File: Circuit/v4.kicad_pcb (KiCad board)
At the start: 2 copper layers, 30 x 50 mm, 41 parts, among them J2 AVR-ISP-6, Q1 IRLML6244TRPBF, U1 HMHA2801AR2, U4 ATtiny841-SSU

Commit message: Version 4.2 complete
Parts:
- moved C2 2.76 mm to (126.7, 63.1)
- moved D1 2.76 mm to (126.7, 60.5)
- moved R5 0.89 mm to (117.2, 57.7)
- moved R16 0.80 mm to (114.1, 57.7)
- moved R19 0.60 mm to (105.8, 74.2)
- moved R6 0.60 mm to (109.6, 69.2)
- moved R7 0.60 mm to (109.6, 79.2)
- moved R8 0.60 mm to (105.1, 69.2)
- moved R9 0.60 mm to (105.1, 79.2)
- moved R10 0.60 mm to (105.1, 61.0)
- moved R12 0.60 mm to (109.6, 61.0)
- moved R11 0.60 mm to (105.1, 87.5)
- moved R13 0.60 mm to (109.6, 87.5)
- moved R20 0.60 mm to (109.4, 74.0)
- moved R17 0.41 mm to (106.9, 55.2)
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- renumbered U4 to ATTINY841
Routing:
- net Net-(Q1-Pad3): track 52.9 -> 39.3 mm, vias 3 -> 2
- net GND: track 56.1 -> 63.7 mm, vias 13 -> 19
- net Net-(ATTINY841-Pad3): track 32.7 -> 30.5 mm
- net DUMP_LOAD_ENABLE: track 16.3 -> 14.9 mm
- net Net-(ATTINY841-Pad2): track 25.2 -> 26.5 mm
- net Net-(ATTINY841-Pad7): track 58.1 -> 59.1 mm
- net 2_VOLT: track 67.3 -> 66.3 mm
- net TXD0: track 17.8 -> 18.5 mm
- net Net-(ATTINY841-Pad9): track 48.2 -> 47.6 mm
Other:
- board text added: "1 Jan 2020"
- board text added: "DIYBMS v4.2"
- board text added: "©2019/2020 Stuart Pittaway"
- board text removed: "20 Dec 2019"
- board text removed: "DIYBMS v4.1"
- board text removed: "©2019 Stuart Pittaway"

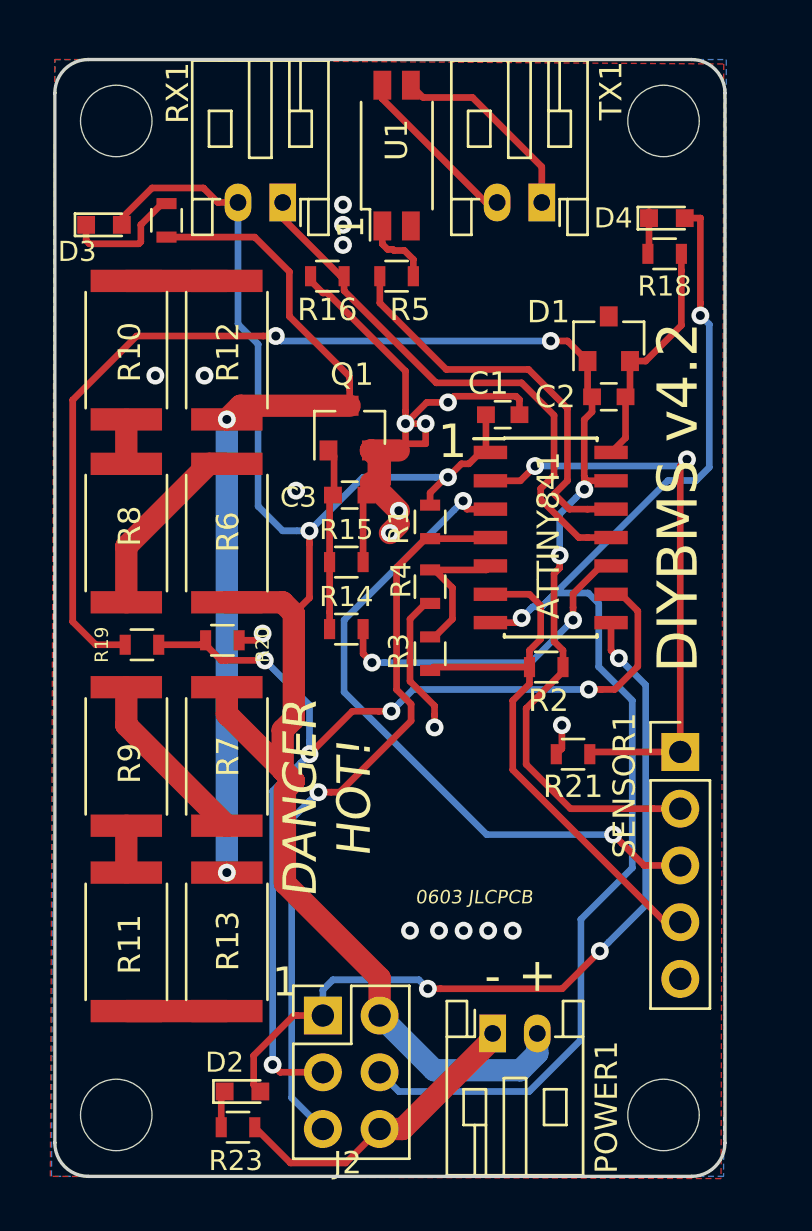
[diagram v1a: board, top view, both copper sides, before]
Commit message: Redesigned circuit using TCLT1003 optoisolator
For 30 boards
Charge Details
Engineering fee:$4.00
Board:$3.10
SMT Price:
Setup fee:$7.00
Stencil:$0.00
Panel:$0.00
Components:$37.27
Extended components fee:$15.00
Total Price:$66.37
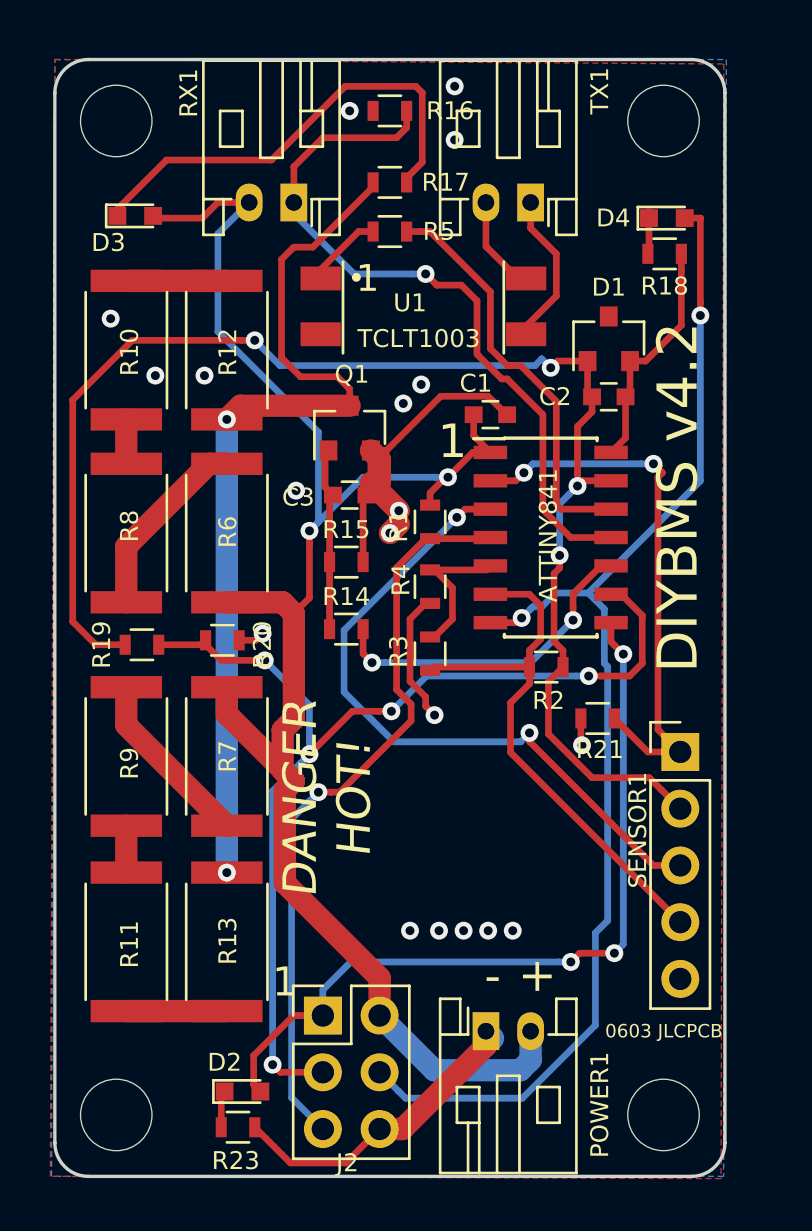
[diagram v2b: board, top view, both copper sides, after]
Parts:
- U1: value HMHA2801AR2 -> TCLT1003; footprint Housings_SSOP:SOP-4_4.4x2.8mm_Pitch1.27mm -> Circuit:SOP4-L-Pitch2.54
- moved R17 10.1 mm to (116.9, 53.5), turned to 0 degrees
- moved R16 7.91 mm to (116.9, 50.3)
- moved U1 6.94 mm to (118.6, 59.1), turned to 270 degrees
- moved R5 2.02 mm to (116.9, 55.7), turned to 0 degrees
- moved R21 1.94 mm to (126.2, 77.5)
- moved D3 1.46 mm to (105.5, 55.0)
- moved C1 0.55 mm to (121.4, 63.9)
- moved RX1 0.50 mm to (112.6, 54.4)
- moved TX1 0.50 mm to (123.2, 54.4)
- moved POWER1 0.32 mm to (121.2, 91.5)
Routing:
- net Net-(D3-Pad1): track 5.55 -> 20.6 mm
- net GND: track 63.7 -> 50.6 mm
- net RXD0: track 24.8 -> 32.7 mm, vias 0 -> 1
- net Net-(TX1-Pad2): track 7.67 -> 4.36 mm
- net Net-(ATTINY841-Pad7): track 59.1 -> 55.9 mm
- net Net-(TX1-Pad1): track 8.97 -> 6.94 mm
- net 2_VOLT: track 66.3 -> 64.5 mm
- net Net-(ATTINY841-Pad2): track 26.5 -> 24.7 mm
- net Net-(Q1-Pad3): track 39.3 -> 40.5 mm
- net Net-(ATTINY841-Pad8): track 36.4 -> 35.6 mm

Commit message: Change components to reduce cost against JLCPCB parts
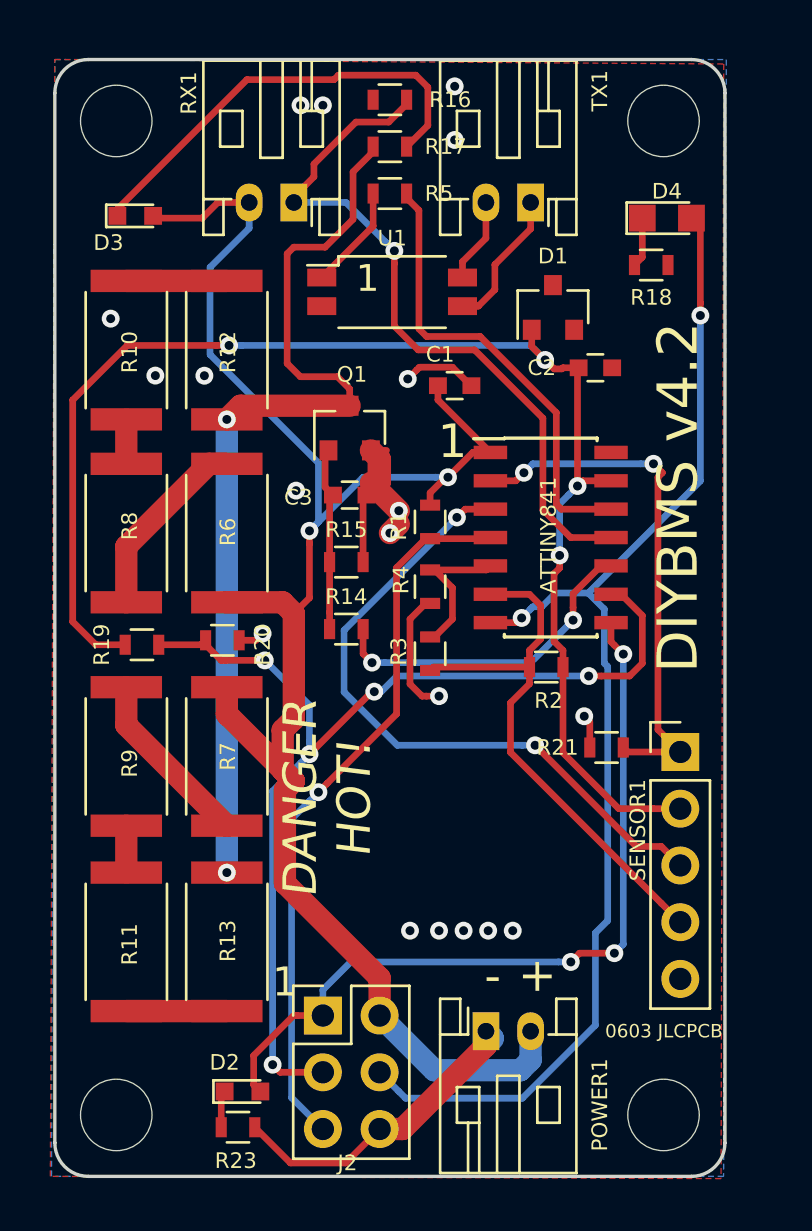
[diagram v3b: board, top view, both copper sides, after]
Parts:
- D4: footprint LEDs:LED_0603 -> LEDs:LED_0805
- U1: value TCLT1003 -> EL3H7(B)(TA)-G; footprint Circuit:SOP4-L-Pitch2.54 -> Housings_SSOP:SOP-4_4.4x2.8mm_Pitch1.27mm
- moved D1 2.87 mm to (124.2, 59.1)
- moved C1 2.06 mm to (119.8, 62.6)
- moved U1 1.75 mm to (117.0, 58.4), turned to 0 degrees
- moved R5 1.70 mm to (116.9, 54.0)
- moved R17 1.60 mm to (116.9, 51.9)
- moved C2 1.43 mm to (126.1, 61.8)
- moved R21 1.36 mm to (126.6, 78.8)
- moved R18 0.78 mm to (128.6, 57.2)
- moved R16 0.50 mm to (116.9, 49.8)
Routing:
- net GND: track 50.6 -> 36.6 mm
- net VCC: track 77.9 -> 80.1 mm
- net TXD0: track 18.5 -> 20.6 mm
- net Net-(Q1-Pad3): track 40.5 -> 42.2 mm
- net Net-(R5-Pad1): track 3.45 -> 4.71 mm
- net Net-(ATTINY841-Pad4): track 33.5 -> 32.4 mm
- net Net-(ATTINY841-Pad2): track 24.7 -> 23.8 mm
- net Net-(D3-Pad1): track 20.6 -> 20.0 mm
- net Net-(TX1-Pad1): track 6.94 -> 6.32 mm
- net Net-(TX1-Pad2): track 4.36 -> 3.79 mm
- net Net-(ATTINY841-Pad3): track 30.4 -> 29.8 mm

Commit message: Changes to parts to keep on JLC basic list and reduce cost
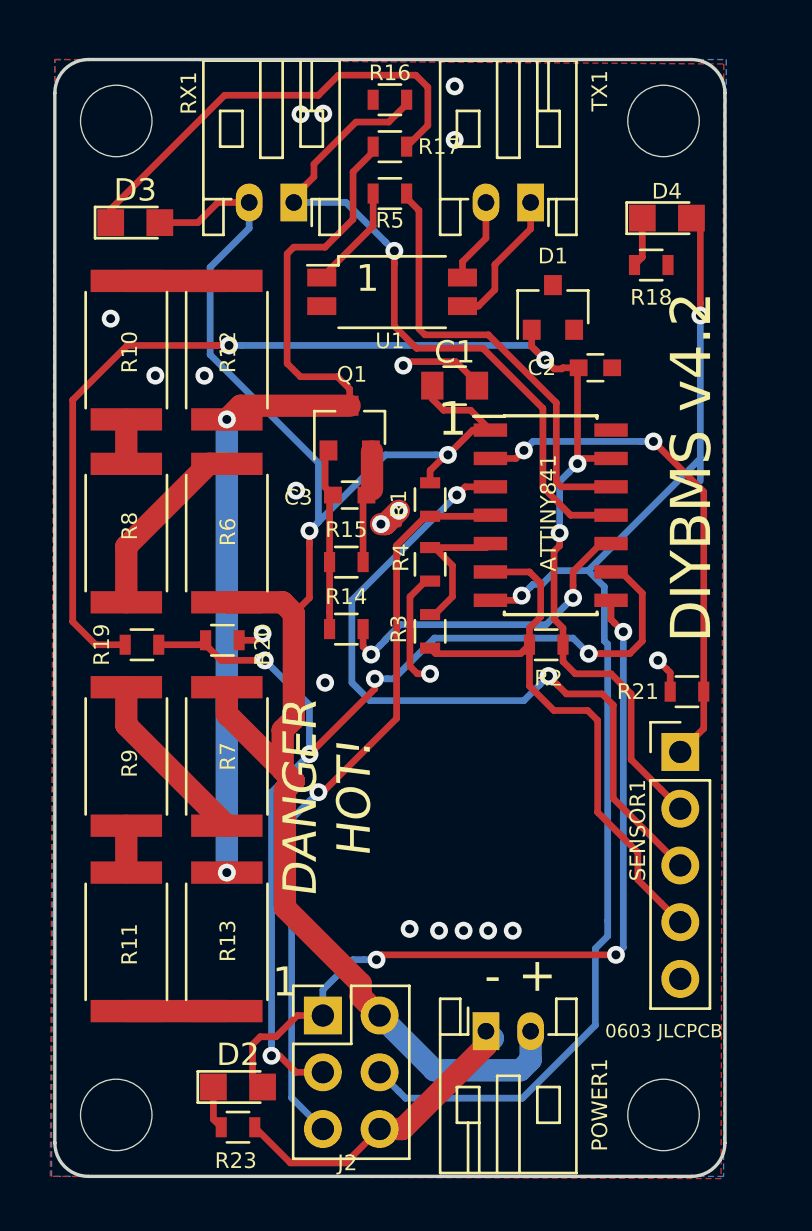
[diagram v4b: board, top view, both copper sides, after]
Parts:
- C1: footprint Capacitors_SMD:C_0603 -> Capacitors_SMD:C_0805
- D2, D3: footprint LEDs:LED_0603 -> LEDs:LED_0805
- moved R21 4.38 mm to (130.2, 76.3)
- moved ATTINY841 1.00 mm to (124.1, 68.4)
- moved R1 1.00 mm to (118.7, 67.7)
- moved R2 1.00 mm to (123.9, 74.2)
- moved R3 1.00 mm to (118.7, 73.6)
- moved R4 1.00 mm to (118.7, 70.6)
- moved D3 0.30 mm to (105.5, 55.3)
- moved D2 0.28 mm to (110.1, 94.0)
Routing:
- net Net-(ATTINY841-Pad3): track 29.8 -> 33.4 mm
- net GND: track 36.6 -> 33.4 mm, vias 19 -> 20
- net ENABLE: track 24.9 -> 26.2 mm
- net Net-(ATTINY841-Pad8): track 35.6 -> 36.9 mm
- net Net-(ATTINY841-Pad4): track 32.4 -> 33.5 mm
- net Net-(ATTINY841-Pad9): track 47.8 -> 48.9 mm
- net Net-(ATTINY841-Pad7): track 55.6 -> 56.6 mm
- net Net-(ATTINY841-Pad2): track 23.8 -> 22.9 mm
- net TXD0: track 20.6 -> 19.9 mm
- net RXD0: track 32.3 -> 31.6 mm
- net 2_VOLT: track 64.2 -> 63.5 mm
- net Net-(D3-Pad1): track 20.0 -> 20.6 mm

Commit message: changed D1 and Q1 orientation
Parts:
- turned D1 to 270 degrees
- turned Q1 to 270 degrees
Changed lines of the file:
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@@
       (drillshape 0)
       (scaleselection 1)
-      (outputdirectory "Gerber"))
+      (outputdirectory ""))
   )
   (net 0 "")
@@
   )
   (module TO_SOT_Packages_SMD:SOT-23 (layer F.Cu)
-    (at 124.2176 59.0876 90)
+    (at 124.2176 59.0876 270)
     (descr "SOT-23, Standard")
     (tags SOT-23)
@@
     (fp_line (start 0.76 -1.58) (end -1.4 -1.58) (layer F.SilkS) (width 0.12))
     (fp_line (start 0.76 1.58) (end -0.7 1.58) (layer F.SilkS) (width 0.12))
-    (pad 1 smd rect (at -1 -0.95 90) (size 0.9 0.8) (layers F.Cu F.Paste F.Mask)
+    (pad 1 smd rect (at -1 -0.95 270) (size 0.9 0.8) (layers F.Cu F.Paste F.Mask)
       (net 16 2_VOLT))
-    (pad 2 smd rect (at -1 0.95 90) (size 0.9 0.8) (layers F.Cu F.Paste F.Mask)
-      (net 1 GND))
-    (pad 3 smd rect (at 1 0 90) (size 0.9 0.8) (layers F.Cu F.Paste F.Mask))
+    (pad 2 smd rect (at -1 0.95 270) (size 0.9 0.8) (layers F.Cu F.Paste F.Mask)
+      (net 1 GND))
+    (pad 3 smd rect (at 1 0 270) (size 0.9 0.8) (layers F.Cu F.Paste F.Mask))
     (model ${KISYS3DMOD}/TO_SOT_Packages_SMD.3dshapes/SOT-23.wrl
       (at (xyz 0 0 0))
@@
   )
   (module TO_SOT_Packages_SMD:SOT-23 (layer F.Cu)
-    (at 115.1176 64.4876 90)
+    (at 115.1176 64.4876 270)
     (descr "SOT-23, Standard")
     (tags SOT-23)
@@
     (fp_line (start 0.76 -1.58) (end -1.4 -1.58) (layer F.SilkS) (width 0.12))
     (fp_line (start 0.76 1.58) (end -0.7 1.58) (layer F.SilkS) (width 0.12))
-    (pad 1 smd rect (at -1 -0.95 90) (size 0.9 0.8) (layers F.Cu F.Paste F.Mask)
+    (pad 1 smd rect (at -1 -0.95 270) (size 0.9 0.8) (layers F.Cu F.Paste F.Mask)
       (net 18 "Net-(C3-Pad1)"))
-    (pad 2 smd rect (at -1 0.95 90) (size 0.9 0.8) (layers F.Cu F.Paste F.Mask)
-      (net 1 GND))
-    (pad 3 smd rect (at 1 0 90) (size 0.9 0.8) (layers F.Cu F.Paste F.Mask)
+    (pad 2 smd rect (at -1 0.95 270) (size 0.9 0.8) (layers F.Cu F.Paste F.Mask)
+      (net 1 GND))
+    (pad 3 smd rect (at 1 0 270) (size 0.9 0.8) (layers F.Cu F.Paste F.Mask)
       (net 13 "Net-(Q1-Pad3)"))
     (model ${KISYS3DMOD}/TO_SOT_Packages_SMD.3dshapes/SOT-23.wrl

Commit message: Ready for use...
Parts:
- ATTINY841: footprint Housings_SOIC:SOIC-14_3.9x8.7mm_Pitch1.27mm -> Package_SO:SOIC-14_3.9x8.7mm_P1.27mm
- C1: footprint Capacitors_SMD:C_0805 -> Capacitor_SMD:C_0805_2012Metric
- C2, C3: footprint Capacitors_SMD:C_0603 -> Capacitor_SMD:C_0603_1608Metric
- D1, Q1: footprint TO_SOT_Packages_SMD:SOT-23 -> Package_TO_SOT_SMD:SOT-23
- D2, D3, D4: footprint LEDs:LED_0805 -> LED_SMD:LED_0805_2012Metric
- J2: footprint Pin_Headers:Pin_Header_Straight_2x03_Pitch2.54mm -> Connector_PinHeader_2.54mm:PinHeader_2x03_P2.54mm_Vertical
- POWER1, RX1, TX1: footprint Connectors_JST:JST_PH_S2B-PH-K_02x2.00mm_Angled -> Connector_JST:JST_PH_S2B-PH-K_1x02_P2.00mm_Horizontal
- R1, R14, R15, R16, R17, R18, R19, R2, R20, R21, R23, R5: footprint Resistors_SMD:R_0603 -> Resistors_SMD:R_0603_1608Metric
- R10, R11, R12, R13, R6, R7, R8, R9: footprint Resistors_SMD:R_2512 -> Resistors_SMD:R_2512_6332Metric
- R3: value 470KOHMS ±1% 1/10W -> 470KOHMS 1% 1/10W; footprint Resistors_SMD:R_0603 -> Resistors_SMD:R_0603_1608Metric
- R4: value 390KOHMS ±1% 1/10W -> 390KOHMS 1% 1/10W; footprint Resistors_SMD:R_0603 -> Resistors_SMD:R_0603_1608Metric
- SENSOR1: footprint Pin_Headers:Pin_Header_Straight_1x05_Pitch2.54mm -> Connector_PinHeader_2.54mm:PinHeader_1x05_P2.54mm_Vertical
- U1: footprint Housings_SSOP:SOP-4_4.4x2.8mm_Pitch1.27mm -> Package_SO:SOP-4_4.4x2.6mm_P1.27mm
- moved R18 0.81 mm to (128.6, 58.0)
- moved D4 0.74 mm to (128.7, 55.5)
- turned D1 to 90 degrees
- turned Q1 to 90 degrees
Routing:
- net Net-(ATTINY841-Pad7): track 56.6 -> 59.8 mm
